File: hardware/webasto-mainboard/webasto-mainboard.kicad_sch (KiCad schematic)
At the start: 10 parts, among them J1 Console FTDI, J2 DEBUG, Q1 DMG2301L, U1 CY15E004J, U2 Pico, U3 LM4040DBZ-2.0

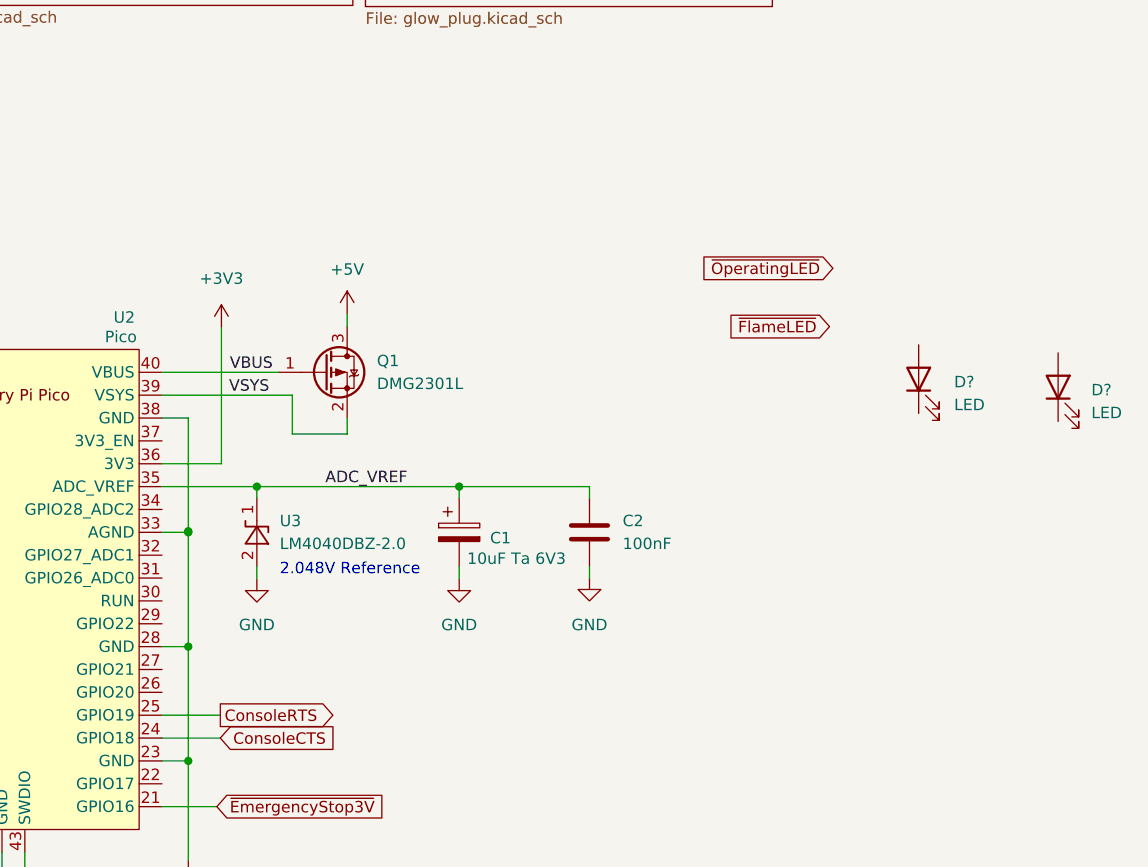
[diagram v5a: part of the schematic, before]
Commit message: Added the LEDs onto the board and init
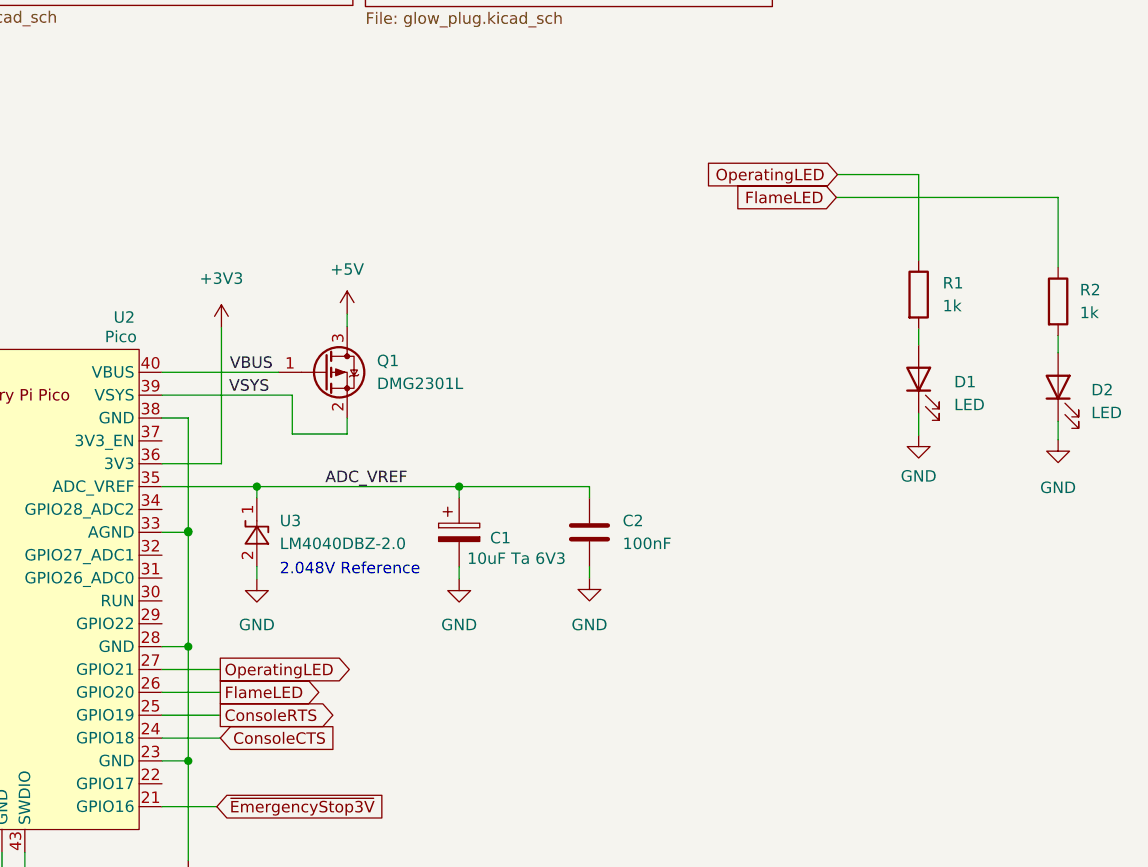
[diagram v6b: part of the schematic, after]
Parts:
- added R1, R2: 1k, Resistor_SMD:R_0805_2012Metric_Pad1.20x1.40mm_HandSolder, symbol Device:R
- D1, D2: renamed from D?; footprint (none) -> LED_SMD:LED_0805_2012Metric_Pad1.15x1.40mm_HandSolder
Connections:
- net GND: now also D1.1 (K), D2.1 (K)
- net FlameLED: now reaches U2.26 (GPIO20)
- net FlameLED: now also R2.1
- net OperatingLED: now reaches U2.27 (GPIO21)
- net OperatingLED: now also R1.1
- net at D1.2 (A): now also R1.2
- net at D2.2 (A): now also R2.2

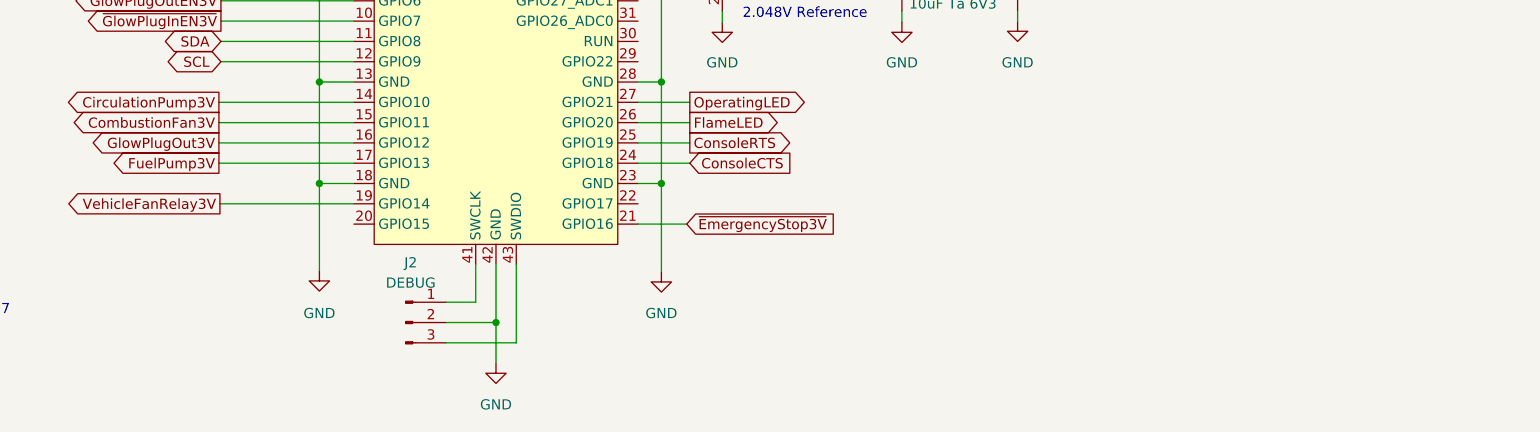
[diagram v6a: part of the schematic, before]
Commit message: Filled out most of the rest (all?) of the FSM
- added a piezo for alarms  (like overheat!)
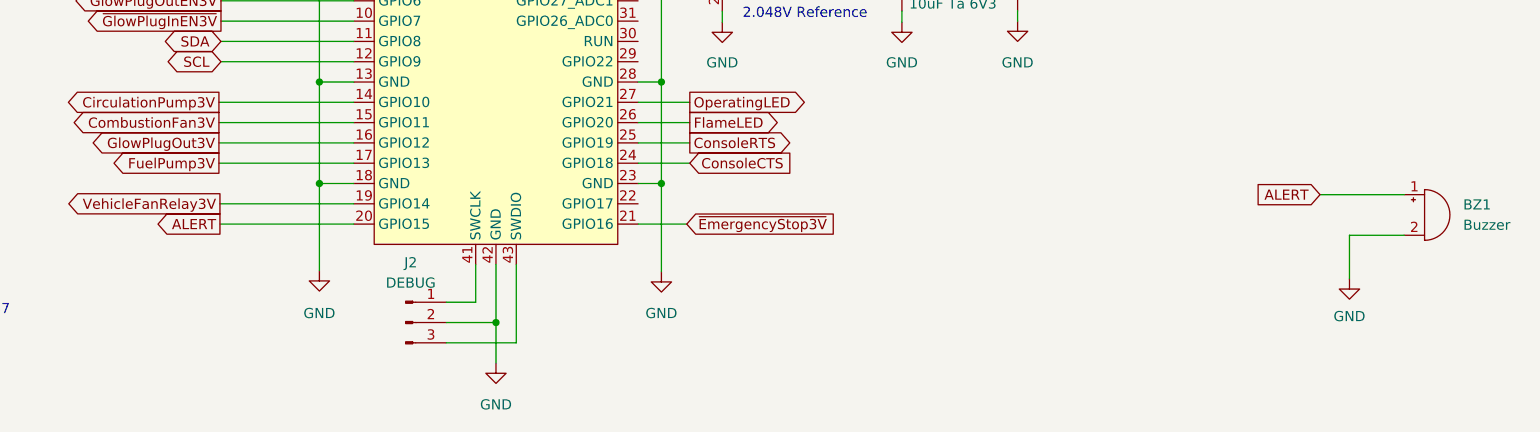
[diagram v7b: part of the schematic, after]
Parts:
- added BZ1: Buzzer, Buzzer_Beeper:Buzzer_TDK_PS1240P02BT_D12.2mm_H6.5mm, symbol Device:Buzzer
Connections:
- net GND: now also BZ1.2 (+)
- net ALERT: now reaches U2.20 (GPIO15)
- net ALERT: now also BZ1.1 (-)

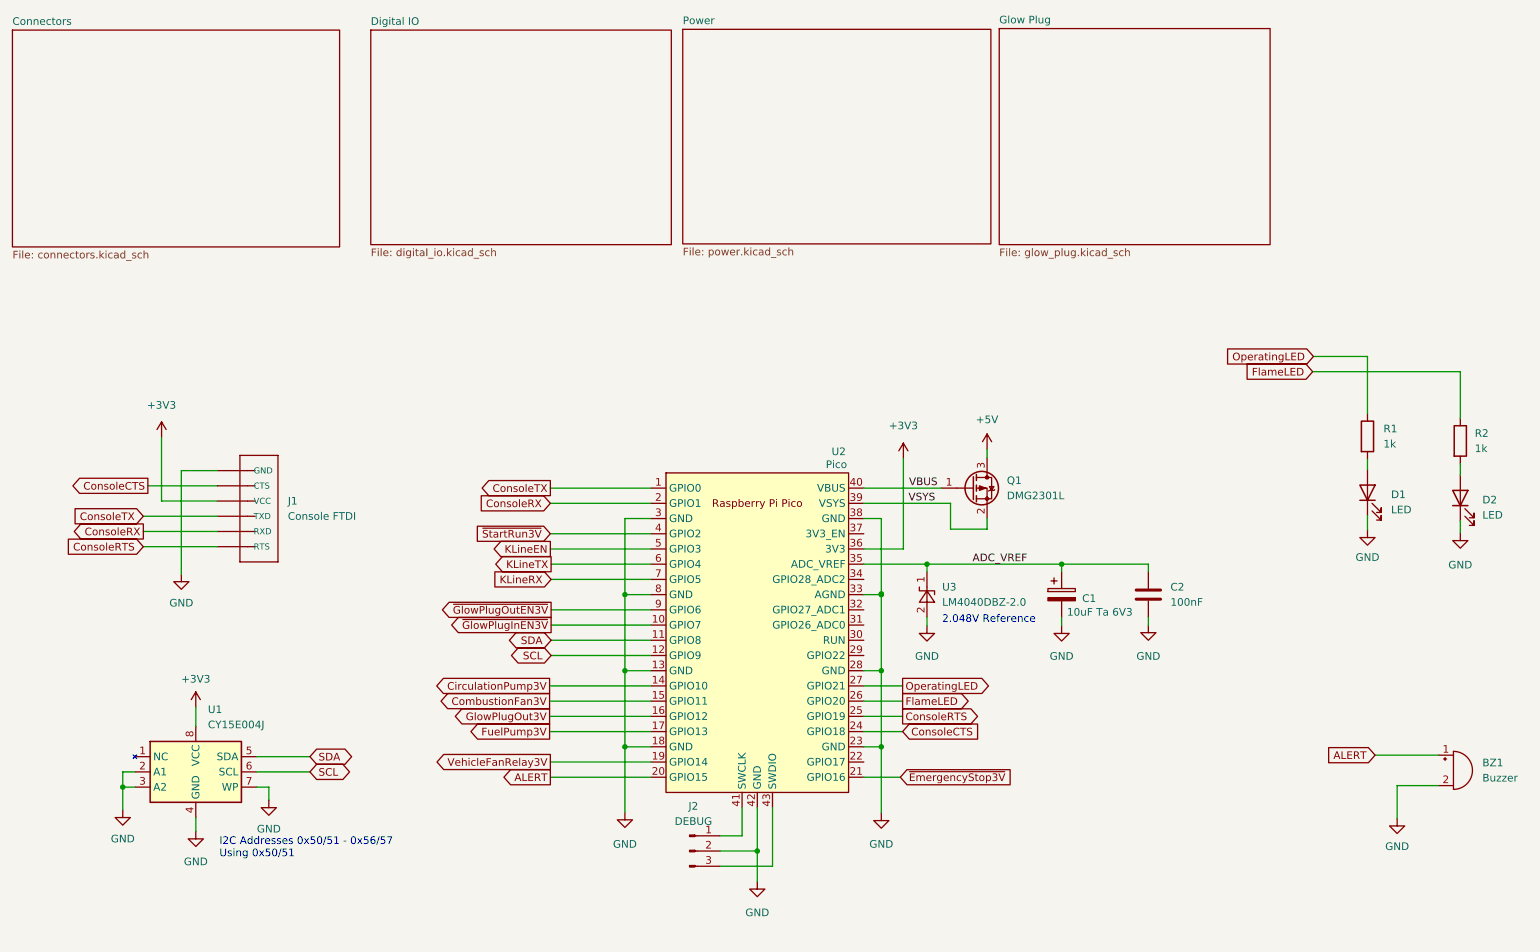
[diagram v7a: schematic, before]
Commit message: Added "USE_USB" input to choose console
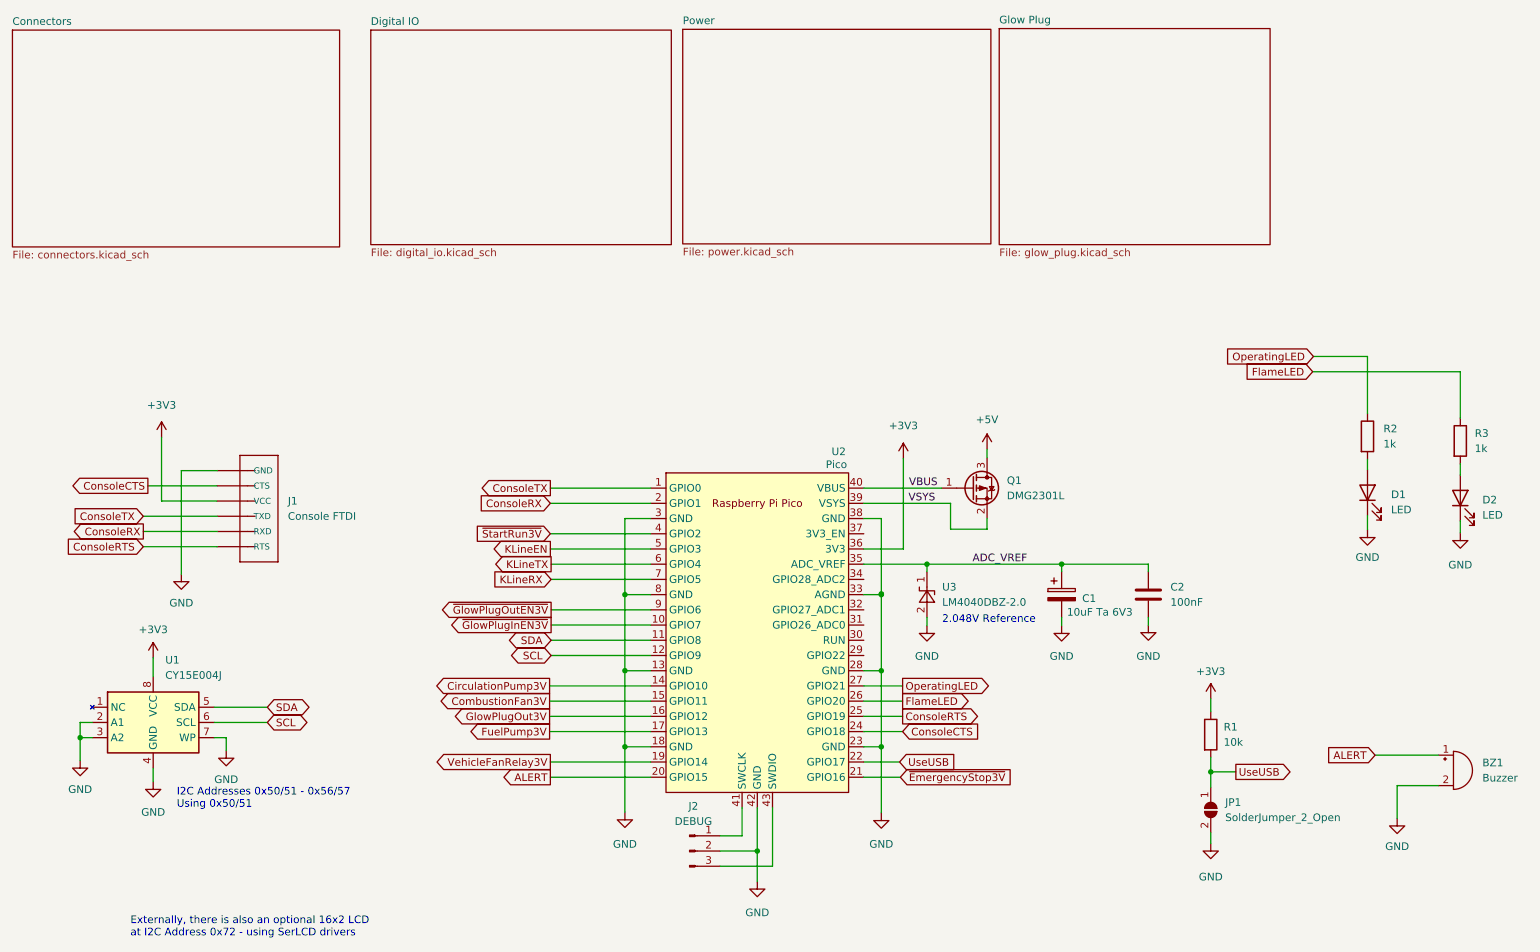
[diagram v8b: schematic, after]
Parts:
- added JP1: SolderJumper_2_Open, Jumper:SolderJumper-2_P1.3mm_Open_TrianglePad1.0x1.5mm, symbol Jumper:SolderJumper_2_Open
- added R1: 10k, Resistor_SMD:R_0805_2012Metric_Pad1.20x1.40mm_HandSolder, symbol Device:R
- renumbered R1 to R2, R2 to R3
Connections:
- net +3V3: now also R1.1
- net GND: now also JP1.2 (B)
- net UseUSB: now reaches U2.22 (GPIO17)
- net UseUSB: now also JP1.1 (A), R1.2
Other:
- note added: "Externally, there is also an optional 16x2 LCD at I2C Address 0x72 - using SerLCD drivers"
- moved on the sheet: U1
